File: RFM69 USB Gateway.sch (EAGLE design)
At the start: 22 parts, among them CN1 MINIB, IC3 MCP1703CB, U1 FT231XS, X1 16 MHz

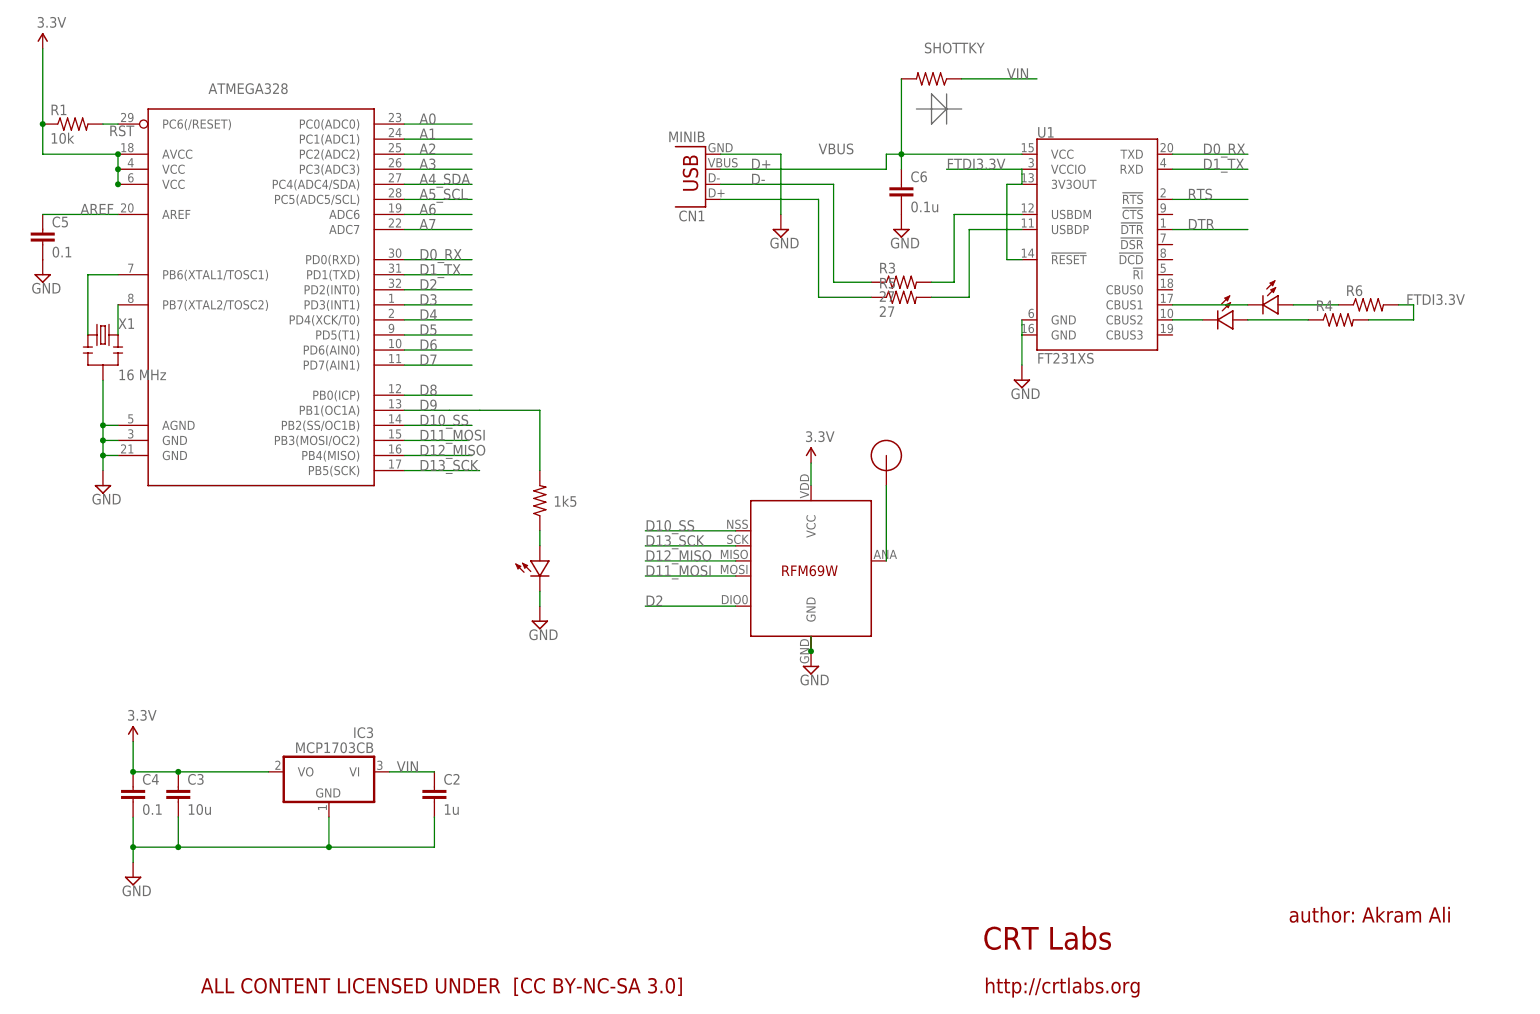
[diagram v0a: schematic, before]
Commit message: Added ISP header and reset button
v0.4
- ISP header
- Reset button
- Silk screen for all components
- Slight rearrangement
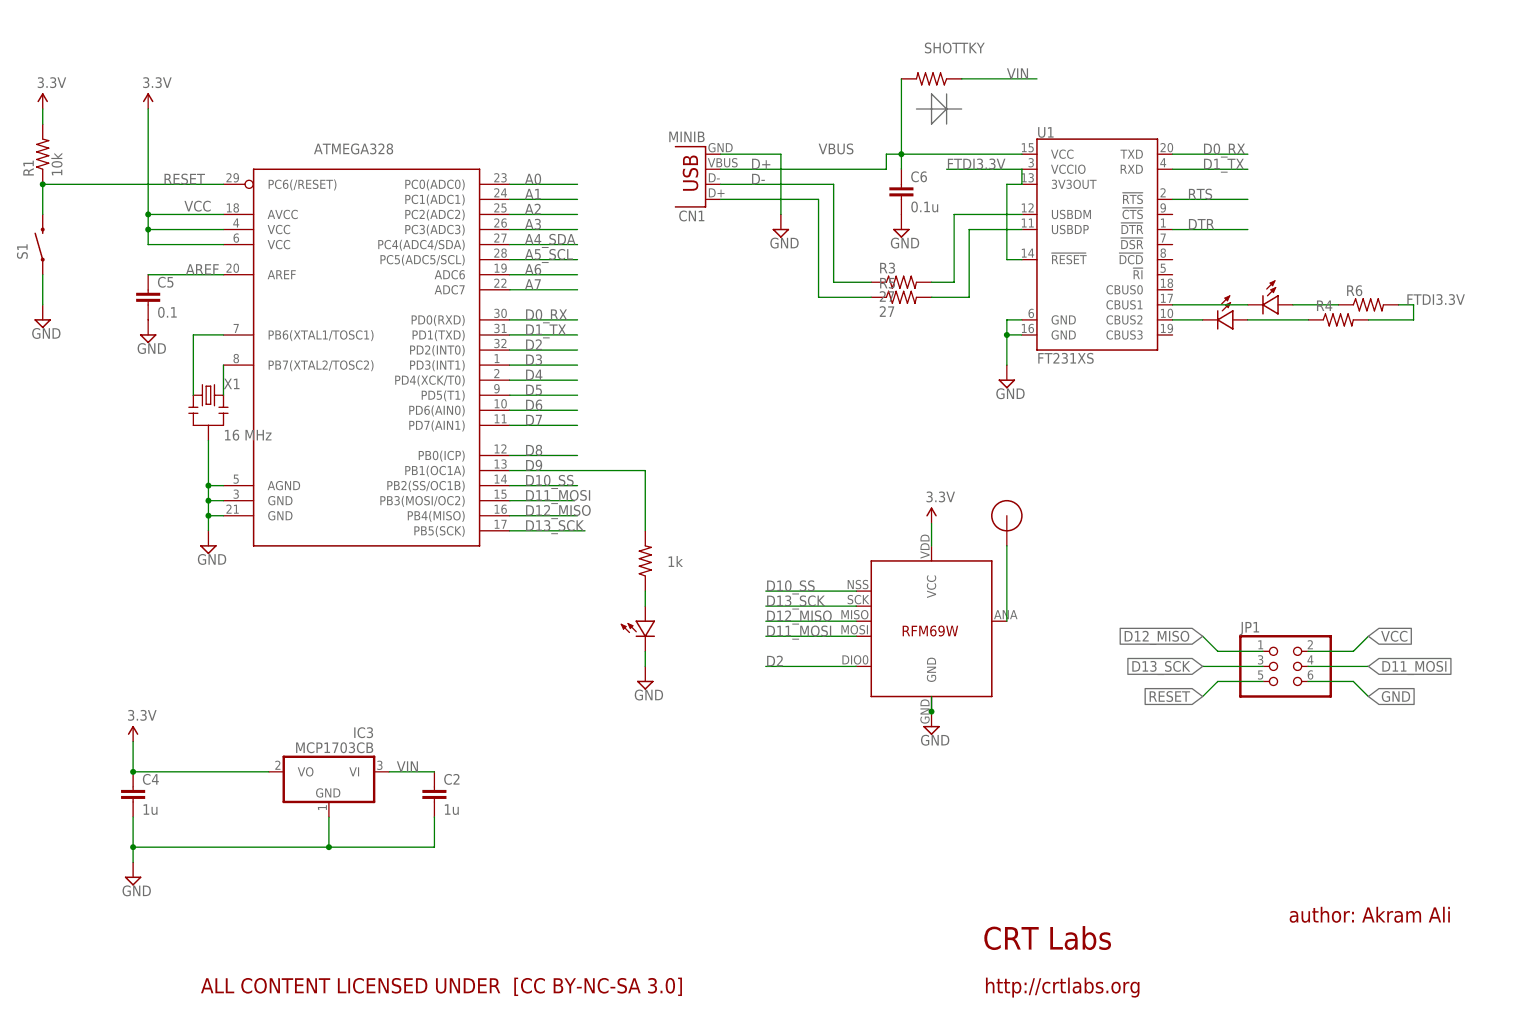
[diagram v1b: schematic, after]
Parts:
- removed C3: 10u, LowPowerLab:CAP0805-CAP
- added JP1: (no value), pinhead:PINHD-2X3
- added S1: SWITCH-MOMENTARY-2SMD-ALT01, Testing:SWITCH-MOMENTARY-2SMD-ALT01
- C4: value 0.1 -> 1u
- R2: value 1k5 -> 1k
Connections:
- removed net RST: ATMEGA328.PC6(/RESET), R1.2
- new net RESET: ATMEGA328.PC6(/RESET), JP1.5, R1.1, S1.2
- net D11_MOSI: now also JP1.4
- net D12_MISO: now also JP1.1
- net D13_SCK: now also JP1.3
- net GND: now also JP1.6, S1.1; no longer C3.2
- net VCC: now also JP1.2, R1.2; no longer C3.1, R1.1
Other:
- moved on the sheet: ATMEGA328, C5, R1, X1

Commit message: Added pullup on CS (pin 10)
10K pullup on CS (RFM69) to avoid issues during ISP programming
Changed all components to 0805 size
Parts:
- added R7: 10K, SparkFun:RESISTOR0805-RES
- C2, C5, C6: device LowPowerLab:CAP0603-CAP -> SparkFun:CAP0805
- C4: device LowPowerLab:CAP0603-CAP -> LowPowerLab:CAP0805
- D, R1: device LowPowerLab:RESISTOR0603-RES -> LowPowerLab:RESISTOR0805
- R2, R3, R4, R5, R6: device LowPowerLab:RESISTOR0603-RES -> SparkFun:RESISTOR0805-RES
- U$2, U$4, U$7: value LED0603 -> LED0805; device LowPowerLab:LED0603 -> LowPowerLab:LED0805
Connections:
- net D10_SS: now also R7.1
- net VCC: now also R7.2

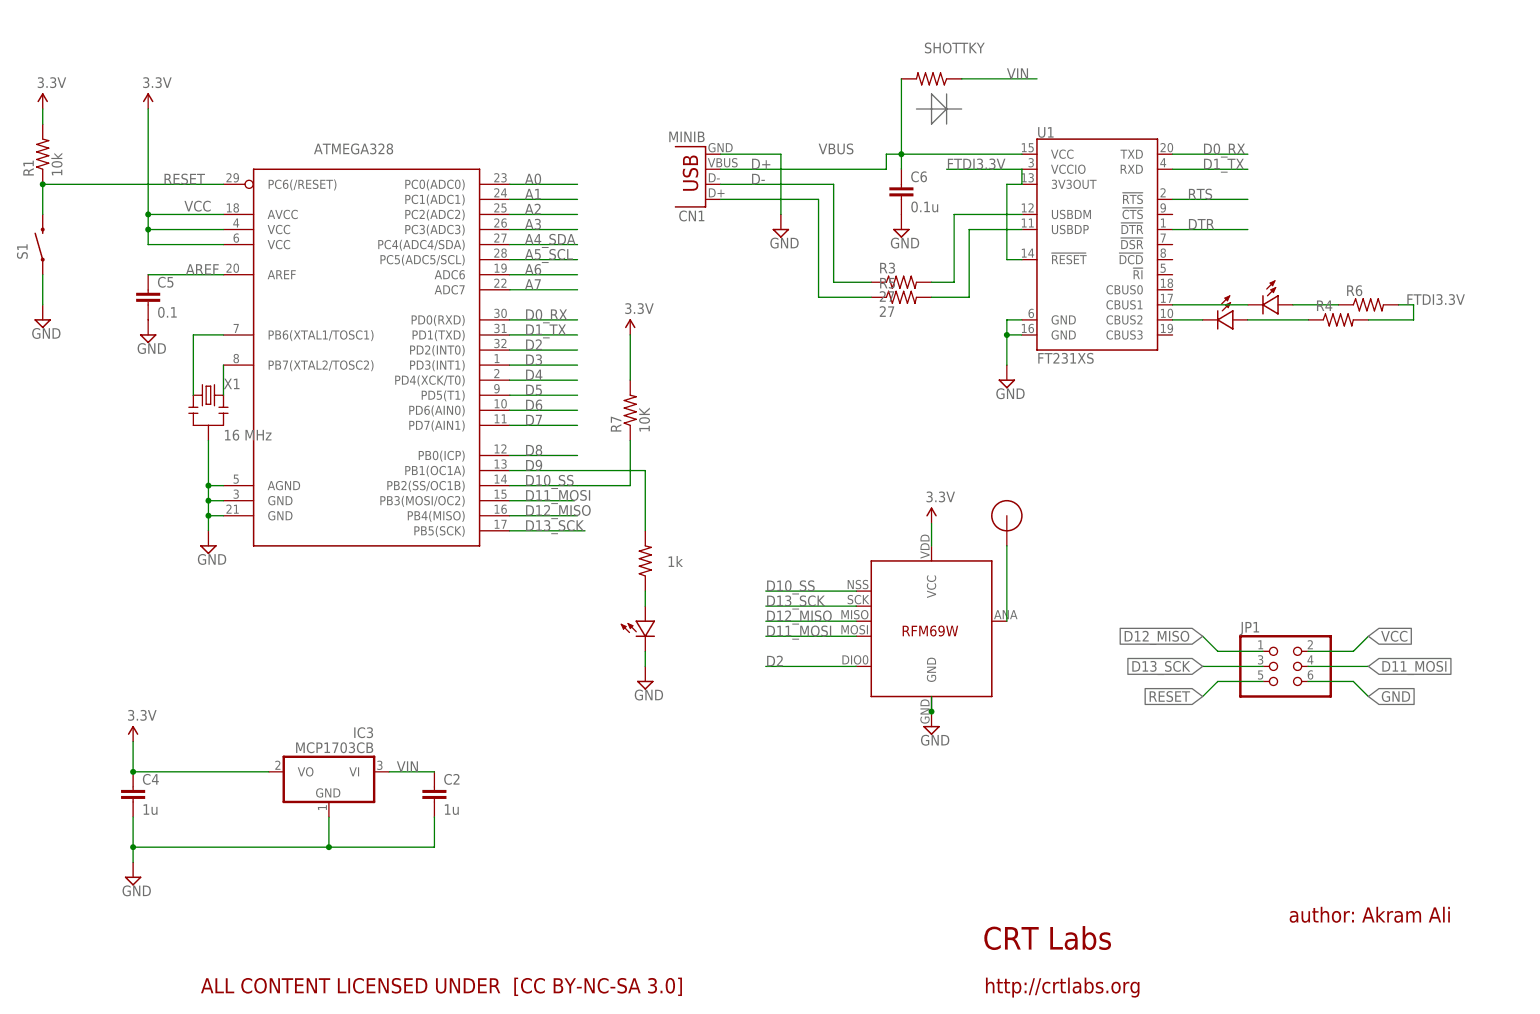
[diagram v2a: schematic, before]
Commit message: v0.6 - fixed auto reset, adjusted traces
Added 0.1 uF cap on reset, series with DTR (allows auto reset via FTDI)
Moved some components to accommodate the cap
Adjusted several traces
Made GND vias more consistent in size
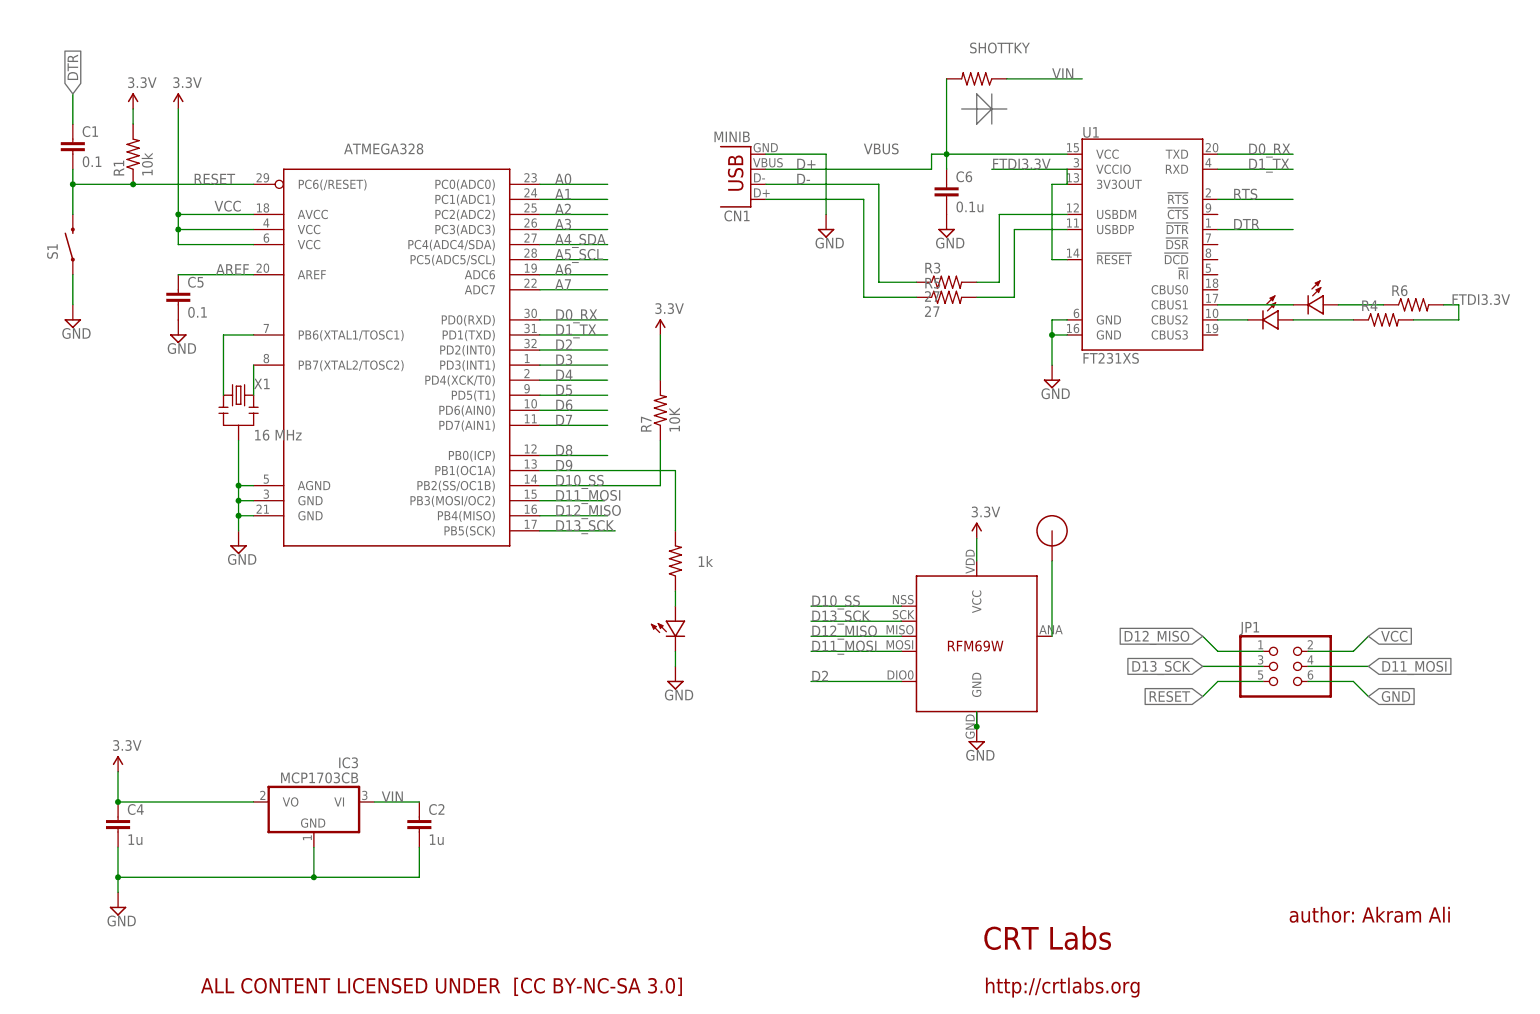
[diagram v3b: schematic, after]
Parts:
- added C1: 0.1, SparkFun:CAP0805
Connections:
- net DTR: now also C1.1
- net RESET: now also C1.2
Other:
- moved on the sheet: ATMEGA328, C2, C4, C5, C6, CN1, IC3, R1, R3, R4, R5, R6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

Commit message: Updated the PDF schematic
v0.6
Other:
- note removed: "ALL CONTENT LICENSED UNDER [CC BY-NC-SA 3.0]"
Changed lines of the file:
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@@
 </classes>
 <parts>
-<part name="FRAME1" library="frames" deviceset="A4L-LOC" device="" value="Moteino"/>
+<part name="FRAME1" library="frames" deviceset="A4L-LOC" device="" value="RFM69 USB Gateway"/>
 <part name="SUPPLY4" library="SparkFun" deviceset="VCC" device="" value="3.3V"/>
 <part name="SUPPLY5" library="supply2" deviceset="GND" device=""/>
@@
 <sheets>
 <sheet>
+<description>RFM 69 USB Gateway</description>
 <plain>
 <text x="166.116" y="15.748" size="3.81" layer="94" font="vector" ratio="10">CRT Labs</text>
@@
 <wire x1="167.64" y1="160.02" x2="167.64" y2="154.94" width="0.1524" layer="96"/>
 <wire x1="162.56" y1="157.48" x2="170.18" y2="157.48" width="0.1524" layer="96"/>
-<text x="34.29" y="8.382" size="2.54" layer="94" font="vector">ALL CONTENT LICENSED UNDER  [CC BY-NC-SA 3.0]</text>
 </plain>
 <instances>
